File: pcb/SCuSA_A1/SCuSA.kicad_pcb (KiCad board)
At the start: 2 copper layers, 51 x 42 mm, 70 parts, among them J101 USB4135-GF-A, J102 JST_S2B-PH-K-x, J103 Binding_Post_PK4_Red, J104 Binding_Post_PK4_Black, J105 SMA_Straight_Jack_Female, J107 77311-118-02LF, J108 77311-118-02LF, Q101 DMN2041LSD, SW101 JS202011CQN, SW102 JS202011CQN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

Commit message: Edit PCB layout
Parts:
- JP103: value SolderJumper_3_Bridged12 -> SolderJumper_3_Open; footprint Jumper:SolderJumper-3_P1.3mm_Bridged12_Pad1.0x1.5mm_NumberLabels -> Jumper:SolderJumper-3_P2.0mm_Open_TrianglePad1.0x1.5mm_NumberLabels
- U104: footprint Package_SON:WSON-12-1EP_3x2mm_P0.5mm_EP1x2.65_ThermalVias -> Package_SON_User:WSON-12-1EP_3x2mm_P0.5mm_EP1x2.65_ThermalVias
- moved TP103 17.0 mm to (147.0, 86.0)
- moved TP108 13.8 mm to (168.7, 77.0)
- moved TP105 11.0 mm to (145.0, 90.0)
- moved TP104 8.94 mm to (138.0, 101.0)
- moved D102 7.15 mm to (127.8, 83.9)
- moved D103 7.10 mm to (127.8, 86.1), turned to 180 degrees
- moved R117 6.95 mm to (127.8, 88.0)
- moved R109 6.01 mm to (127.8, 81.8), turned to 0 degrees
- moved SW102 5.60 mm to (136.0, 84.2)
- moved JP103 5.48 mm to (139.6, 91.8), turned to 180 degrees
- moved R120 5.46 mm to (132.0, 83.7)
- moved U103 4.37 mm to (127.8, 79.1), turned to 90 degrees
- moved C114 2.66 mm to (135.2, 94.6)
- moved R118 1.92 mm to (150.8, 78.8)
- moved J105 1.58 mm to (158.0, 74.5)
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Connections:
- net Net-(J103-Pad1) renamed /SNS+1
- net Net-(J104-Pad1) renamed /SNS-1
- net Net-(U105-IN+) renamed /SNS+2
- net Net-(U105-IN-) renamed /SNS-2
- C109 pad 1: GND -> -Vx
- C111 pad 2: GND -> -Vx
- C112 pad 2: -VOffset -> -Vx
- C113 pad 2: -VOffset -> -Vx
- JP103 pad 2: -VOffset -> -Vx
- RV101 pad 3: -VOffset -> -Vx
- TP103 pad 1: -VOffset -> -Vx
- U105 pad 2: -VOffset -> -Vx
- U106 pad 4: -VOffset -> -Vx
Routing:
- net +3V3: track 2.91 -> 45.7 mm
- net /VBat_SW: track 0.00 -> 38.7 mm, vias 0 -> 1
- net Net-(SW102A-C): track 0.00 -> 19.8 mm
- net /-2V_filt: track 0.00 -> 12.8 mm
- net Net-(SW102B-B): track 0.00 -> 12.4 mm
- net -Vx: track 0.00 -> 12.0 mm, vias 0 -> 11
- net GND: track 2.78 -> 14.6 mm, vias 2 -> 8
- net /SNS-1: track 0.00 -> 11.5 mm
- net /SNS+1: track 0.00 -> 10.9 mm
- net /Out: track 0.00 -> 10.2 mm
- net Net-(SW102A-B): track 0.00 -> 8.34 mm
- net /PGOOD: track 12.0 -> 4.85 mm
- net Net-(U106--): track 0.00 -> 5.48 mm
- net /SNS-2: track 0.00 -> 4.86 mm
- net /SNS+2: track 0.00 -> 4.86 mm
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- added copper zone on B.Cu, net -Vx
- added copper zone on F.Cu, net -Vx
- added copper zone on B.Cu, net GND
- added copper zone on F.Cu, net GND

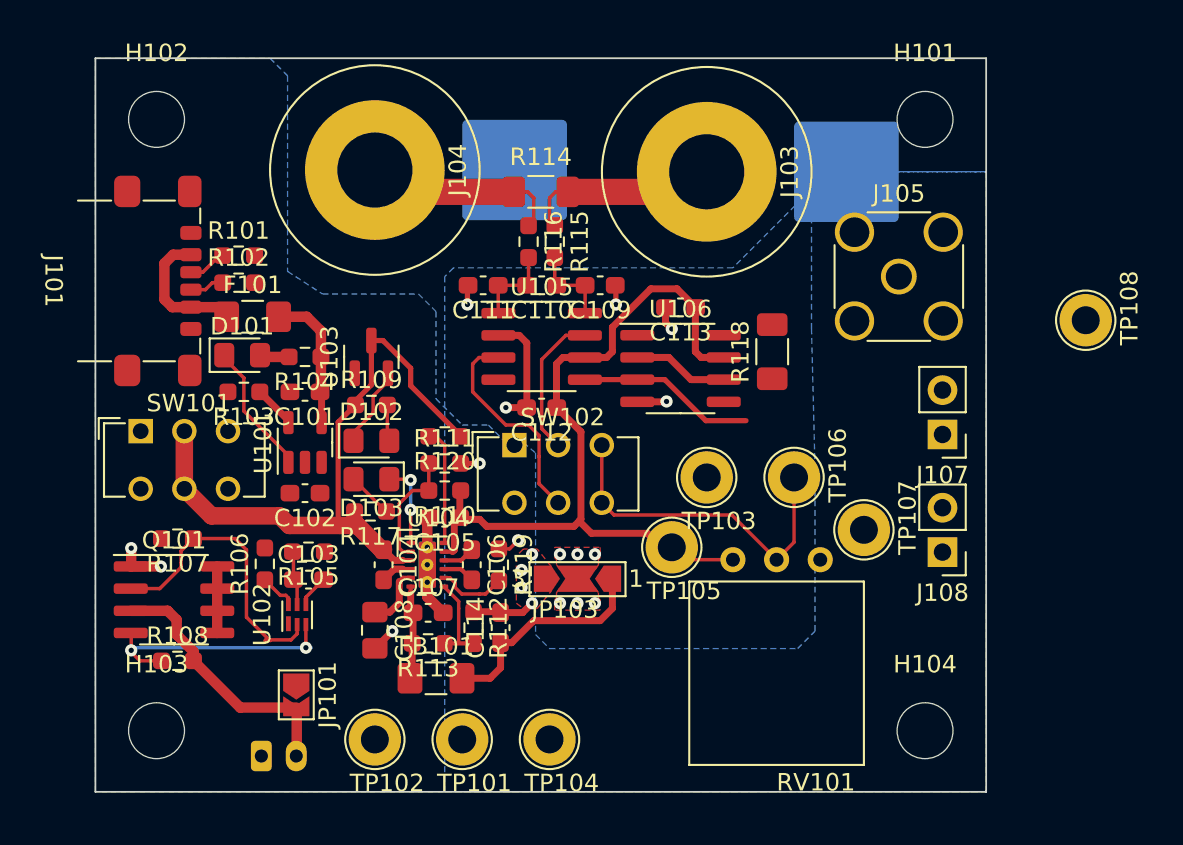
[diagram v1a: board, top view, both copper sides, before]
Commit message: Change binding posts and GND planes
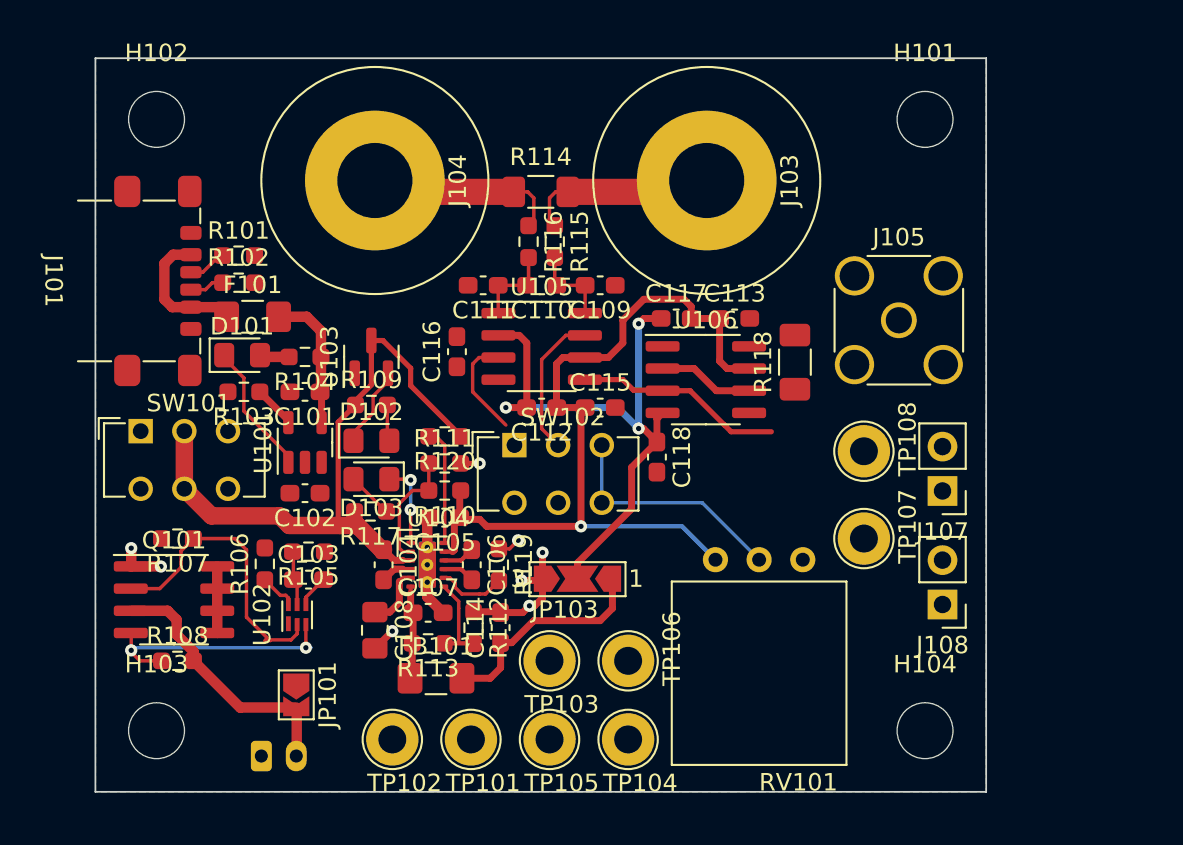
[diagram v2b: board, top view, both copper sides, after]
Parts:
- added C115: 100nF,16V,X7R,0603, Capacitor_SMD:C_0603_1608Metric_Pad1.08x0.95mm_HandSolder, F.Cu at (140.9, 82.0)
- added C116: 100nF,16V,X7R,0603, Capacitor_SMD:C_0603_1608Metric_Pad1.08x0.95mm_HandSolder, F.Cu at (132.7, 78.8)
- added C117: 100nF,16V,X7R,0603, Capacitor_SMD:C_0603_1608Metric_Pad1.08x0.95mm_HandSolder, F.Cu at (145.2, 76.9)
- added C118: 100nF,16V,X7R,0603, Capacitor_SMD:C_0603_1608Metric_Pad1.08x0.95mm_HandSolder, F.Cu at (144.2, 84.8)
- J103: value Binding_Post_PK4_Red -> Binding_Post_PKI_10_A_Au; footprint Connector_User:Binding_Post_PK4_Red -> Connector_User:Binding_Post_PKI_10_A_Au_Red
- J104: value Binding_Post_PK4_Black -> Binding_Post_PKI_10_A_Au; footprint Connector_User:Binding_Post_PK4_Black -> Connector_User:Binding_Post_PKI_10_A_Au_Black
- moved TP108 14.7 mm to (156.0, 84.5)
- moved TP106 14.2 mm to (142.5, 96.5)
- moved TP103 13.8 mm to (138.0, 96.5)
- moved TP105 13.0 mm to (138.0, 101.0)
- moved TP104 4.50 mm to (142.5, 101.0)
- moved J107 3.23 mm to (160.5, 86.8)
- moved C113 3.16 mm to (148.6, 76.9), turned to 0 degrees
- moved J108 3.00 mm to (160.5, 93.3)
- moved J105 2.50 mm to (158.0, 77.0)
- moved U106 1.58 mm to (146.9, 80.4)
- moved R118 1.43 mm to (152.1, 79.4)
- moved RV101 1.00 mm to (150.0, 90.7)
- moved TP102 1.00 mm to (129.0, 101.0)
- moved J104 0.60 mm to (128.0, 69.0)
- moved J103 0.50 mm to (147.0, 69.0)
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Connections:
- C109 pad 1: -Vx -> GND
- C111 pad 2: -Vx -> GND
- C113 pad 2: -Vx -> GND
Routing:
- net -Vx: track 12.0 -> 35.1 mm, vias 11 -> 3
- net Net-(SW102B-B): track 12.4 -> 5.91 mm
- net Net-(SW102A-C): track 19.8 -> 13.7 mm
- net GND: track 14.6 -> 19.2 mm, vias 8 -> 7
- net +3V3: track 45.7 -> 47.6 mm, vias 0 -> 1
- net /Out: track 10.2 -> 11.9 mm
- net /SNS-1: track 11.5 -> 10.8 mm
- removed copper zone on B.Cu, net -Vx
- removed copper zone on F.Cu, net -Vx
- removed copper zone on F.Cu, net GND

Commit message: Edit PCB layout
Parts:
- removed TP103, TP105: TestPoint_5010_Red, TestPoint:TestPoint_Loop_D2.60mm_Drill1.6mm_Beaded
- added C119: 1uF,16V,X7R,0603, Capacitor_SMD:C_0603_1608Metric_Pad1.08x0.95mm_HandSolder, F.Cu at (141.8, 91.5)
- added FB100: 742792620, Inductor_SMD:L_1206_3216Metric_Pad1.42x1.75mm_HandSolder, F.Cu at (138.5, 90.5)
- moved TP106 11.2 mm to (148.5, 87.0)
- moved SW101 6.51 mm to (119.6, 87.5), turned to 180 degrees
- moved TP104 4.50 mm to (138.0, 101.0)
- moved TP107 4.00 mm to (156.0, 93.5)
- moved JP103 3.23 mm to (138.4, 94.8), turned to 90 degrees
- moved J108 1.50 mm to (160.5, 94.8)
- moved RV101 1.50 mm to (148.5, 90.7)
- moved TP108 1.50 mm to (156.0, 86.0)
- moved C118 1.41 mm to (145.2, 83.9), turned to 0 degrees
- moved R106 1.25 mm to (121.6, 92.2)
- moved J105 1.00 mm to (158.0, 78.0)
- moved J107 0.38 mm to (160.5, 87.2)
- moved J102 0.30 mm to (121.5, 101.7)
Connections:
- C105 pad 1: +3V3 -> Net-(U104-OUT+)
- R110 pad 1: +3V3 -> Net-(U104-OUT+)
- U104 pad 11: +3V3 -> Net-(U104-OUT+)
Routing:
- net /VBat: track 0.00 -> 41.9 mm
- net GND: track 19.2 -> 46.4 mm, vias 7 -> 23
- net /VBat_SW: track 38.7 -> 64.9 mm, vias 1 -> 3
- net -Vx: track 35.1 -> 51.2 mm
- net /Out: track 11.9 -> 25.9 mm
- net /Cell-: track 17.0 -> 31.0 mm
- net Net-(U104-OUT+): track 0.00 -> 9.39 mm
- net +3V3: track 47.6 -> 38.8 mm
- net Net-(SW102B-B): track 5.91 -> 12.4 mm
- net Net-(J105-In): track 0.00 -> 6.01 mm
- net /-2V_filt: track 12.8 -> 7.65 mm
- net Net-(U106--): track 5.48 -> 8.14 mm
- net Net-(SW102A-C): track 13.7 -> 14.7 mm
- net Net-(U102-V-): track 2.15 -> 1.52 mm
- net Net-(Q101A-G1): track 16.9 -> 16.3 mm
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
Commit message: Fix errors, edit PCB layout
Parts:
- added C120: 100nF,16V,X7R,0603, Capacitor_SMD:C_0603_1608Metric_Pad1.08x0.95mm_HandSolder, F.Cu at (130.6, 80.9)
- added G***: Sense_Logo, Logo_User:Sense_Logo, F.Cu at (137.5, 65.0)
- C101, C102: footprint Capacitor_SMD:C_0603_1608Metric_Pad1.08x0.95mm_HandSolder -> Capacitor_SMD:C_0805_2012Metric_Pad1.18x1.45mm_HandSolder
- moved TP106 0.95 mm to (149.4, 86.7)
- moved C102 0.22 mm to (123.9, 87.1)
- moved C101 0.20 mm to (124.0, 80.9)
- moved R103 0.10 mm to (120.4, 81.1)
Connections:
- U103 pad 1: GND -> Net-(D102-K)
- U103 pad 2: Net-(D102-K) -> GND
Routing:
- net Net-(SW102A-C): track 14.7 -> 16.4 mm
- net /VBat_SW: track 64.9 -> 66.4 mm
- net GND: track 46.4 -> 47.5 mm
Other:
- board text added: "*"
- board text added: "+"
- board text added: "-"
- board text added: "1S Lipo"
- board text added: "GND"
- board text added: "Off/On"
- board text added: "Out"
- board text added: "Out 50 Ω"
- board text added: "PWR"
- board text added: "SCuSA Rev A1"
- board text added: "SNS+"
- board text added: "SNS-"
- board text added: "Trim"

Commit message: Minor SCH and PCB modifications
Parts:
- added C121: C, Capacitor_SMD:C_0603_1608Metric_Pad1.08x0.95mm_HandSolder, F.Cu at (153.0, 83.5)
- added R121: R, Resistor_SMD:R_0603_1608Metric_Pad0.98x0.95mm_HandSolder, F.Cu at (151.5, 83.5)
- U105: value AD8410AWBRZ -> AD8418AWBRZ
- moved G*** 0.32 mm to (137.6, 65.3)
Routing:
- net GND: track 47.5 -> 50.9 mm
- net Net-(U106--): track 8.14 -> 10.0 mm
- net Net-(C121-Pad1): track 0.00 -> 1.52 mm
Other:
- board text added: "**"
- board text added: "-2V to +70V"
- board text added: "Scope Current Sense Amplifier SCuSA - Rev A1 by fl0m0"
- board text removed: "SCuSA Rev A1"

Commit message: RevA1
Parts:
- added R122: 0R,0603, Resistor_SMD:R_0603_1608Metric_Pad0.98x0.95mm_HandSolder, F.Cu at (118.6, 70.1)
- moved J101 0.50 mm to (116.9, 74.8)
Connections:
- J101 pad M: unconnected-(J101-SHIELD-PadM) -> Net-(J101-SHIELD)
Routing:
- net Net-(J101-SHIELD): track 0.00 -> 19.3 mm
- net GND: track 50.9 -> 52.5 mm
- net Net-(J101-CC2): track 1.99 -> 2.49 mm
- net Net-(J101-CC1): track 2.21 -> 2.71 mm
- net Net-(F101-Pad1): track 7.75 -> 8.25 mm
